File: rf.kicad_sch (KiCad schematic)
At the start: 40 parts, among them J16 ANT, J17 Switch Select, J18 Conn_Coaxial, U10 PE4250MLI, U11 0433BM15A0001, U12 RFFM6406, U8 SF2446E, U9 PE4250MLI

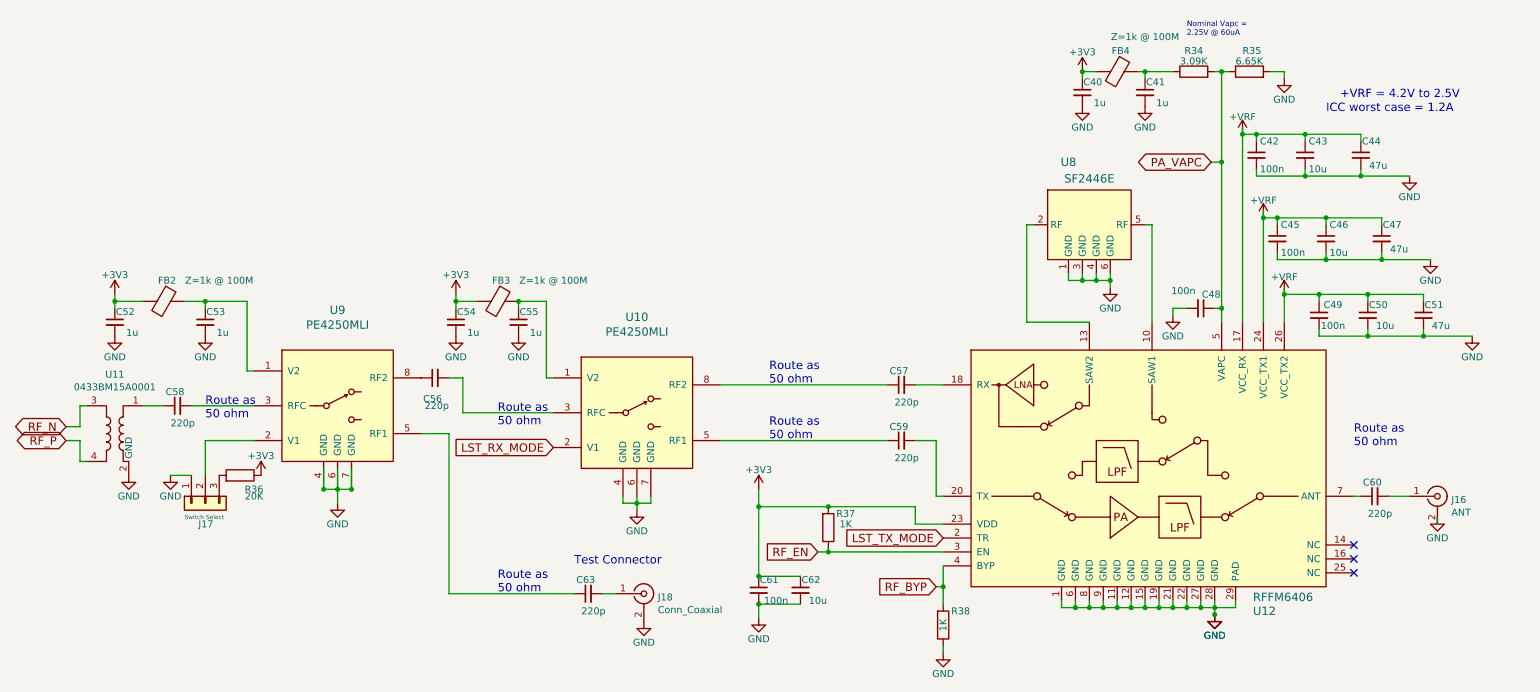
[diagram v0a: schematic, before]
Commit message: automatic schematic and pcb valiadation and cleanup
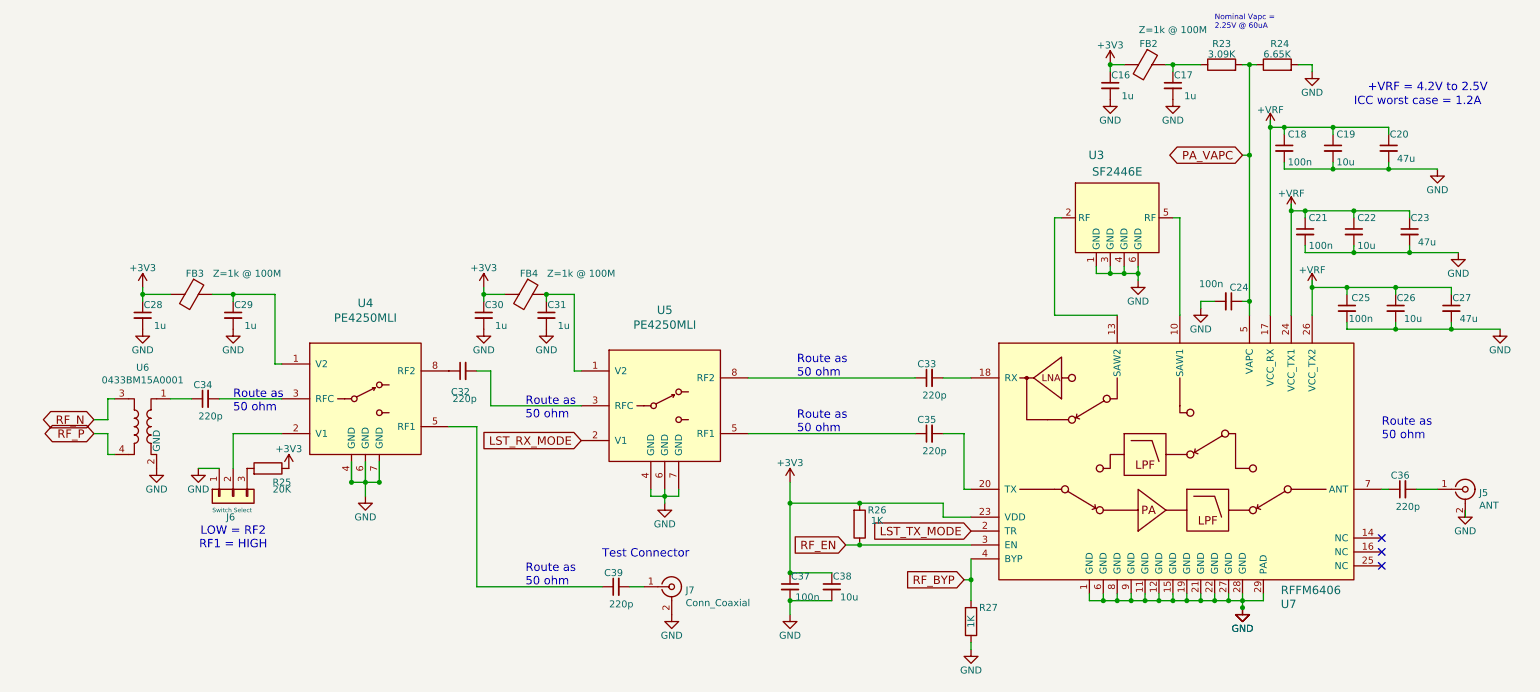
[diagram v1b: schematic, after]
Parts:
- renumbered C40 to C16, C41 to C17, C42 to C18, C43 to C19, C44 to C20, C45 to C21, C46 to C22, C47 to C23, C48 to C24, C49 to C25, C50 to C26, C51 to C27, C52 to C28, C53 to C29, C54 to C30, C55 to C31, C56 to C32, C57 to C33, C58 to C34, C59 to C35, C60 to C36, C61 to C37, C62 to C38, C63 to C39, FB4 to FB2, FB2 to FB3, FB3 to FB4, J16 to J5, J17 to J6, J18 to J7, R34 to R23, R35 to R24, R36 to R25, R37 to R26, R38 to R27, U8 to U3, U9 to U4, U10 to U5, U11 to U6, U12 to U7
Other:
- note added: "LOW = RF2 RF1 = HIGH"
- moved on the sheet: C16, C17, C18, C19, C20, C21, C22, C23, C24, C25, C26, C27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

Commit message: ???
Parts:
- renumbered C39 to C37, C37 to C38, C38 to C39
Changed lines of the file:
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@@
 		(on_board yes)
 		(dnp no)
-		(property "Reference" "C38"
+		(property "Reference" "C39"
 			(at 159.385 133.985 0)
 			(effects
@@
 			(project "openlst-hw"
 				(path "/a863a5ec-a5d4-4f54-be53-e8c01d5e3ac4/d6d0e934-53b0-468d-8d79-aec6d2c37df2"
-					(reference "C38")
+					(reference "C39")
 					(unit 1)
 				)
@@
 		(on_board yes)
 		(dnp no)
-		(property "Reference" "#PWR062"
+		(property "Reference" "#PWR063"
 			(at 149.86 147.32 0)
 			(effects
@@
 			(project "openlst-hw"
 				(path "/a863a5ec-a5d4-4f54-be53-e8c01d5e3ac4/d6d0e934-53b0-468d-8d79-aec6d2c37df2"
-					(reference "#PWR062")
+					(reference "#PWR063")
 					(unit 1)
 				)
@@
 		(on_board yes)
 		(dnp no)
-		(property "Reference" "#PWR063"
+		(property "Reference" "#PWR062"
 			(at 128.27 147.32 0)
 			(effects
@@
 			(project "openlst-hw"
 				(path "/a863a5ec-a5d4-4f54-be53-e8c01d5e3ac4/d6d0e934-53b0-468d-8d79-aec6d2c37df2"
-					(reference "#PWR063")
+					(reference "#PWR062")
 					(unit 1)
 				)
@@
 		(on_board yes)
 		(dnp no)
-		(property "Reference" "C39"
+		(property "Reference" "C37"
 			(at 119.38 133.35 90)
 			(effects
@@
 			(project "openlst-hw"
 				(path "/a863a5ec-a5d4-4f54-be53-e8c01d5e3ac4/d6d0e934-53b0-468d-8d79-aec6d2c37df2"
-					(reference "C39")
+					(reference "C37")
 					(unit 1)
 				)
@@
 		(on_board yes)
 		(dnp no)
-		(property "Reference" "C37"
+		(property "Reference" "C38"
 			(at 151.765 133.985 0)
 			(effects
@@
 			(project "openlst-hw"
 				(path "/a863a5ec-a5d4-4f54-be53-e8c01d5e3ac4/d6d0e934-53b0-468d-8d79-aec6d2c37df2"
-					(reference "C37")
+					(reference "C38")
 					(unit 1)
 				)

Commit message: temporary branch for radio to pc104
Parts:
- renumbered R23 to R19, R24 to R20, R25 to R21, R26 to R22, R27 to R23
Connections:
- net +3V3 renamed 3V3
- net +VRF renamed VRF

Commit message: use Common libraries, replace TI MCU with STM32 for CAN bridge
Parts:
- J5, J7: footprint Project:LINX_CONSMA001-G -> Common:LINX_CONSMA001-G
- U3: footprint Project:SF2446E -> Common:SF2446E
- U7: footprint Project:RFFM6406 -> Common:RFFM6406
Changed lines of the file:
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@@
 			)
 		)
-		(property "Footprint" "Project:SF2446E"
+		(property "Footprint" "Common:SF2446E"
 			(at 209.55 68.58 0)
 			(effects
@@
 			)
 		)
-		(property "Footprint" "Project:RFFM6406"
+		(property "Footprint" "Common:RFFM6406"
 			(at 215.9 107.95 0)
 			(effects
@@
 			)
 		)
-		(property "Footprint" "Project:LINX_CONSMA001-G"
+		(property "Footprint" "Common:LINX_CONSMA001-G"
 			(at 273.05 118.11 0)
 			(effects
@@
 			)
 		)
-		(property "Footprint" "Project:LINX_CONSMA001-G"
+		(property "Footprint" "Common:LINX_CONSMA001-G"
 			(at 128.27 135.89 0)
 			(effects
